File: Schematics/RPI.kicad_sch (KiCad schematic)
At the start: 9 parts, among them J1 RPi GPIO, U2 24LC256

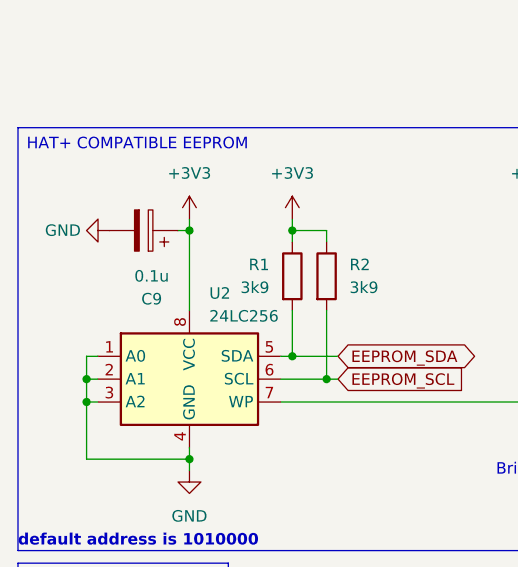
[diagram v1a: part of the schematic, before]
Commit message: Changed footprints, added 3d model to GPIO
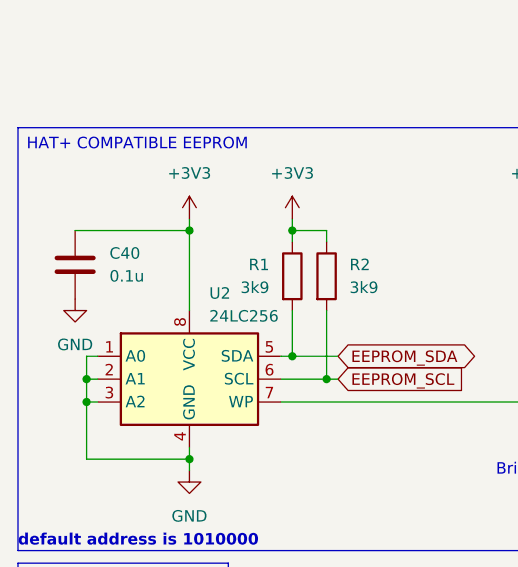
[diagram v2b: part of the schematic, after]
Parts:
- removed C9: 0.1u, Capacitor_SMD:C_0805_2012Metric_Pad1.18x1.45mm_HandSolder, symbol Device:C_Polarized
- added C40: 0.1u, Capacitor_SMD:C_0805_2012Metric_Pad1.18x1.45mm_HandSolder, symbol Device:C
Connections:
- net +3V3: now also C40.1
- net GND: now also C40.2
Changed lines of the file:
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@@
 	(wire
 		(pts
-			(xy 146.05 34.29) (xy 151.13 34.29)
+			(xy 22.86 55.88) (xy 35.56 55.88)
 		)
 		(stroke
@@
 	(wire
 		(pts
-			(xy 163.83 29.21) (xy 166.37 29.21)
+			(xy 146.05 34.29) (xy 151.13 34.29)
 		)
 		(stroke
@@
 	(wire
 		(pts
-			(xy 151.13 39.37) (xy 148.59 39.37)
+			(xy 163.83 29.21) (xy 166.37 29.21)
 		)
 		(stroke
@@
 	(wire
 		(pts
-			(xy 163.83 64.77) (xy 166.37 64.77)
+			(xy 151.13 39.37) (xy 148.59 39.37)
 		)
 		(stroke
@@
 	(wire
 		(pts
-			(xy 24.13 69.85) (xy 24.13 72.39)
+			(xy 163.83 64.77) (xy 166.37 64.77)
 		)
 		(stroke
@@
 	(wire
 		(pts
-			(xy 34.29 55.88) (xy 35.56 55.88)
+			(xy 24.13 69.85) (xy 24.13 72.39)
 		)
 		(stroke
@@
 	)
 	(symbol
-		(lib_id "Device:C_Polarized")
-		(at 30.48 55.88 270)
-		(mirror x)
-		(unit 1)
-		(exclude_from_sim no)
-		(in_bom yes)
-		(on_board yes)
-		(dnp no)
-		(property "Reference" "C9"
-			(at 31.369 63.5 90)
-			(effects
-				(font
-					(size 1.27 1.27)
-				)
-			)
-		)
-		(property "Value" "0.1u"
-			(at 31.369 60.96 90)
-			(effects
-				(font
-					(size 1.27 1.27)
-				)
-			)
-		)
-		(property "Footprint" "Capacitor_SMD:C_0805_2012Metric_Pad1.18x1.45mm_HandSolder"
-			(at 26.67 54.9148 0)
-			(effects
-				(font
-					(size 1.27 1.27)
-				)
-				(hide yes)
-			)
-		)
-		(property "Datasheet" "~"
-			(at 30.48 55.88 0)
-			(effects
-				(font
-					(size 1.27 1.27)
-				)
-				(hide yes)
-			)
-		)
-		(property "Description" "Polarized capacitor"
-			(at 30.48 55.88 0)
-			(effects
-				(font
-					(size 1.27 1.27)
-				)
-				(hide yes)
-			)
-		)
-		(pin "2"
-		)
-		(pin "1"
-		)
-		(instances
-			(project "Harmoniser HAT"
-				(path "/41751dd2-97f9-4cc6-b9e6-b561e5949053/94150540-adfd-4870-80d6-c5485bc02207"
-					(reference "C9")
-					(unit 1)
-				)
-			)
-		)
-	)
-	(symbol
 		(lib_id "power:+5V")
 		(at 166.37 27.94 0)
@@
 	)
 	(symbol
-		(lib_id "power:GND")
-		(at 26.67 55.88 270)
+		(lib_id "Device:R")
+		(at 22.86 118.11 180)
 		(unit 1)
 		(exclude_from_sim no)
@@
 		(on_board yes)
 		(dnp no)
-		(fields_autoplaced yes)
-		(property "Reference" "#PWR013"
-			(at 20.32 55.88 0)
+		(property "Reference" "R5"
+			(at 25.908 117.856 0)
 			(effects
 				(font
 					(size 1.27 1.27)
 				)
-				(hide yes)
 			)
 		)
-		(property "Value" "GND"
-			(at 23.495 55.8799 90)
+		(property "Value" "10k"
+			(at 22.86 118.11 90)
 			(effects
 				(font
 					(size 1.27 1.27)
 				)
-				(justify right)
 			)
 		)
-		(property "Footprint" ""
-			(at 26.67 55.88 0)
+		(property "Footprint" "Resistor_SMD:R_0805_2012Metric_Pad1.20x1.40mm_HandSolder"
+			(at 24.638 118.11 90)
 			(effects
 				(font
@@
 			)
 		)
-		(property "Datasheet" ""
-			(at 26.67 55.88 0)
+		(property "Datasheet" "~"
+			(at 22.86 118.11 0)
 			(effects
 				(font
@@
 			)
 		)
-		(property "Description" "Power symbol creates a global label with name \"GND\" , ground"
-			(at 26.67 55.88 0)
+		(property "Description" "Resistor"
+			(at 22.86 118.11 0)
 			(effects
 				(font
@@
 		(pin "1"
 		)
+		(pin "2"
+		)
 		(instances
 			(project "Harmoniser HAT"
 				(path "/41751dd2-97f9-4cc6-b9e6-b561e5949053/94150540-adfd-4870-80d6-c5485bc02207"
-					(reference "#PWR013")
+					(reference "R5")
 					(unit 1)
 				)
@@
 	(symbol
 		(lib_id "Device:R")
-		(at 22.86 118.11 180)
+		(at 22.86 106.68 180)
 		(unit 1)
 		(exclude_from_sim no)
@@
 		(on_board yes)
 		(dnp no)
-		(property "Reference" "R5"
-			(at 25.908 117.856 0)
+		(property "Reference" "R4"
+			(at 26.416 106.553 0)
 			(effects
 				(font
@@
 			)
 		)
-		(property "Value" "10k"
-			(at 22.86 118.11 90)
+		(property "Value" "22k"
+			(at 22.86 106.68 90)
 			(effects
 				(font
@@
 		)
 		(property "Footprint" "Resistor_SMD:R_0805_2012Metric_Pad1.20x1.40mm_HandSolder"
-			(at 24.638 118.11 90)
+			(at 24.638 106.68 90)
 			(effects
 				(font
@@
 		)
 		(property "Datasheet" "~"
-			(at 22.86 118.11 0)
+			(at 22.86 106.68 0)
 			(effects
 				(font
@@
 		)
 		(property "Description" "Resistor"
-			(at 22.86 118.11 0)
+			(at 22.86 106.68 0)
 			(effects
 				(font
@@
 			(project "Harmoniser HAT"
 				(path "/41751dd2-97f9-4cc6-b9e6-b561e5949053/94150540-adfd-4870-80d6-c5485bc02207"
-					(reference "R5")
+					(reference "R4")
 					(unit 1)
 				)
@@
 	)
 	(symbol
-		(lib_id "Device:R")
-		(at 22.86 106.68 180)
+		(lib_id "Device:C")
+		(at 22.86 59.69 0)
 		(unit 1)
 		(exclude_from_sim no)
@@
 		(on_board yes)
 		(dnp no)
-		(property "Reference" "R4"
-			(at 26.416 106.553 0)
+		(fields_autoplaced yes)
+		(property "Reference" "C40"
+			(at 26.67 58.4199 0)
 			(effects
 				(font
 					(size 1.27 1.27)
 				)
+				(justify left)
 			)
 		)
-		(property "Value" "22k"
-			(at 22.86 106.68 90)
+		(property "Value" "0.1u"
+			(at 26.67 60.9599 0)
 			(effects
 				(font
 					(size 1.27 1.27)
 				)
+				(justify left)
 			)
 		)
-		(property "Footprint" "Resistor_SMD:R_0805_2012Metric_Pad1.20x1.40mm_HandSolder"
-			(at 24.638 106.68 90)
+		(property "Footprint" "Capacitor_SMD:C_0805_2012Metric_Pad1.18x1.45mm_HandSolder"
+			(at 23.8252 63.5 0)
 			(effects
 				(font
@@
 		)
 		(property "Datasheet" "~"
-			(at 22.86 106.68 0)
+			(at 22.86 59.69 0)
 			(effects
 				(font
@@
 			)
 		)
-		(property "Description" "Resistor"
-			(at 22.86 106.68 0)
+		(property "Description" "Unpolarized capacitor"
+			(at 22.86 59.69 0)
 			(effects
 				(font
@@
 			(project "Harmoniser HAT"
 				(path "/41751dd2-97f9-4cc6-b9e6-b561e5949053/94150540-adfd-4870-80d6-c5485bc02207"
-					(reference "R4")
+					(reference "C40")
 					(unit 1)
 				)
@@
 					(unit 1)
 				)
+			)
+		)
+	)
+	(symbol
+		(lib_id "power:GND")
+		(at 22.86 63.5 0)
+		(unit 1)
+		(exclude_from_sim no)
+		(in_bom yes)
+		(on_board yes)
+		(dnp no)
+		(fields_autoplaced yes)
+		(property "Reference" "#PWR070"
+			(at 22.86 69.85 0)
+			(effects
+				(font
+					(size 1.27 1.27)
+				)
+				(hide yes)
+			)
+		)
+		(property "Value" "GND"
+			(at 22.86 68.58 0)
+			(effects
+				(font
+					(size 1.27 1.27)
+				)
+			)
+		)
+		(property "Footprint" ""
+			(at 22.86 63.5 0)
+			(effects
+				(font
+					(size 1.27 1.27)
+				)
+				(hide yes)
+			)
+		)
+		(property "Datasheet" ""
+			(at 22.86 63.5 0)
+			(effects
+				(font
+					(size 1.27 1.27)
+				)
+				(hide yes)
+			)
+		)
+		(property "Description" "Power symbol creates a global label with name \"GND\" , ground"
+			(at 22.86 63.5 0)
+			(effects
+				(font
+					(size 1.27 1.27)
+				)
+				(hide yes)
+			)
+		)
+		(pin "1"
+		)
+		(instances
+			(project "Harmoniser HAT"
+				(path "/41751dd2-97f9-4cc6-b9e6-b561e5949053/94150540-adfd-4870-80d6-c5485bc02207"
+					(reference "#PWR070")
+					(unit 1)
+				)

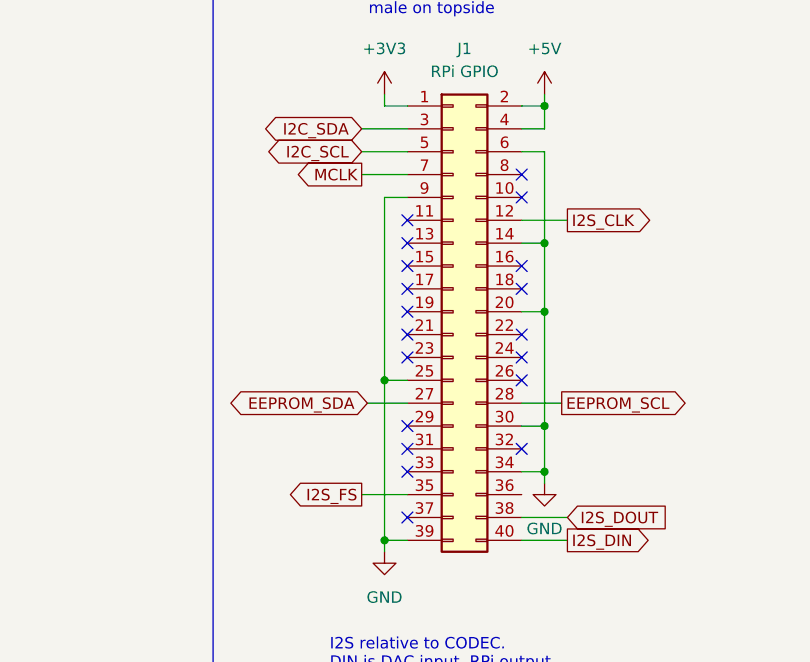
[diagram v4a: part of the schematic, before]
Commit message: Fix for Uni PCB
CODEC module, DIP package, and through-hole less components
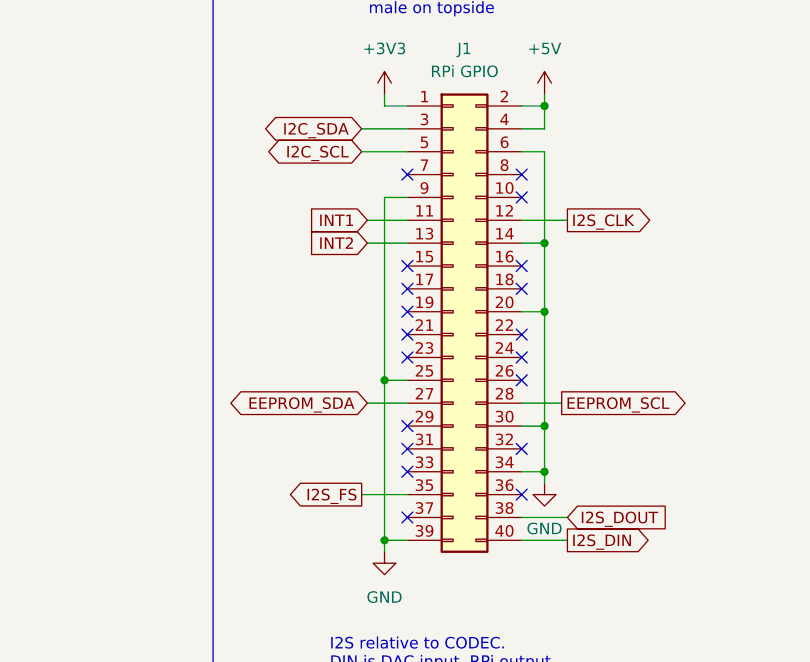
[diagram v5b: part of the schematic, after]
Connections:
- net INT1: now reaches J1.11 (Pin_11)
- net INT2: now reaches J1.13 (Pin_13)
- net MCLK: no longer names the net of J1.7 (Pin_7)
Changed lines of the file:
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@@
 	)
 	(no_connect
+		(at 151.13 36.83)
+	)
+	(no_connect
+		(at 163.83 72.39)
+	)
+	(no_connect
 		(at 163.83 36.83)
 	)
@@
 	)
 	(no_connect
-		(at 151.13 44.45)
-	)
-	(no_connect
 		(at 151.13 49.53)
 	)
@@
 	)
 	(no_connect
-		(at 151.13 41.91)
-	)
-	(no_connect
 		(at 163.83 59.69)
 	)
@@
 	(wire
 		(pts
+			(xy 146.685 41.91) (xy 151.13 41.91)
+		)
+		(stroke
+			(width 0)
+			(type default)
+		)
+	)
+	(wire
+		(pts
 			(xy 22.86 113.03) (xy 27.94 113.03)
 		)
@@
 	(wire
 		(pts
-			(xy 146.05 36.83) (xy 151.13 36.83)
-		)
-		(stroke
-			(width 0)
-			(type default)
-		)
-	)
-	(wire
-		(pts
 			(xy 22.86 110.49) (xy 22.86 113.03)
 		)
@@
 	(wire
 		(pts
+			(xy 146.685 44.45) (xy 151.13 44.45)
+		)
+		(stroke
+			(width 0)
+			(type default)
+		)
+	)
+	(wire
+		(pts
 			(xy 146.685 62.23) (xy 151.13 62.23)
 		)
@@
 			"AAAAAAAAAAAAAAAAAAAAAAAAAAAAAAAAAAAAAAAAAAAAAAAAAAAAAAAAAAAAAAAAAAAAAAAAAAAA"
 			"AAAAAAAAAAAAAAAAAAAAAAAAAAAAAAAAAAAAAAAAAAAAAAAAAAAAAAAAAAAAAAAAAAAAAAAAAAAA"
+			"AAAAAAAAAAAAAAAAAAAAAAAAAAAAAAAAAAAAAAAAAAAAAAAAAAAAAAAAAAAAAAAAAAAAAAAAAAAA"
+			"AAAAAAAAAAAAAAAAAAAAAAAAAAAAAAAAAAAAAAAAAAAAAAAAAAAAAAAAAAAAAAAAAAAAAAAAAAAA"
+			"AAAAAAAAAAAAAAAAAAAAAAAAAAAAAAAAAAAAAAAAAAAAAAAAAAAAAAAAAAAAAAAAAAAAAAAAAAAA"
+			"AAAAAAAAAAAAAAAAAAAAAAAAAAAAAAAAAAAAAAAAAAAAAAAAAAAAAAAAAAAAAAAAAAAAAAAAAAAA"
+			"AAAAAAAAAAAAAAAAAAAAAAAAAAAAAAAAAAAAAAAAAAAAAAAAAAAAAAAAAAAAAAAAAAAAAAAAAAAA"
+			"AAAAAAAAAAAAAAAAAAAAAAAAAAAAAAAAAAAAAAAAAAAAAAAAAAAAAAAAAAAAAAAAAAAAAAAAAAAA"
+			"AAAAAAAAAAAAAAAAAAAAAAAAAAAAAAAAAAAAAAAAAAAAAAAAAAAAAAAAAAAAAAAAAAAAAAAAAAAA"
+			"AAAAAAAAAAAAAAAAAAAAAAAAAAAAAAAAAAAAAAAAAAAAAAAAAAAAAAAAAAAAAAAAAAAAAAAAAAAA"
+			"AAAAAAAAAAAAAAAAAAAAAAAAAAAAAAAAAAAAAAAAAAAAAAAAAAAAAAAAAAAAAAAAAAAAAAAAAAAA"
+			"AAAAAAAAAAAAAAAAAAAAAAAAAAAAAAAAAAAAAAAAAAAAAAAAAAAAAAAAAAAAAAAAAAAAAAAAAAAA"
+			"AAAAAAAAAAAAAAAAAAAAAAAAAAAAAAAAAAAAAAAAAAAAAAAAAAAAAAAAAAAAAAAAAAAAAAAAAAAA"
+			"AAAAAAAAAAAAAAAAAAAAAAAAAAAAAAAAAAAAAAAAAAAAAAAAAAAAAAAAAAAAAAAAAAAAAAAAAAAA"
+			"AAAAAAAAAAAAAAAAAAAAAAAAAAAAAAAAAAAAAAAAAAAAAAAAAAAAAAAAAAAAAAAAAAAAAAAAAAAA"
+			"AAAAAAAAAAAAAAAAAAAAAAAAAAAAAAAAAAAAAAAAAAAAAAAAAAAAAAAAAAAAAAAAAAAAAAAAAAAA"
+			"AAAAAAAAAAAAAAAAAAAAAAAAAAAAAAAAAAAAAAAAAAAAAAAAAAAAAAAAAAAAAAAAAAAAAAAAAAAA"
+			"AAAAAAAAAAAAAAAAAAAAAAAAAAAAAAAAAAAAAAAAAAAAAAAAAAAAAAAAAAAAAAAAAAAAAAAAAAAA"
+			"AAAAAAAAAAAAAAAAAAAAAAAAAAAAAAAAAAAAAAAAAAAAAAAAAAAAAAAAAAAAAAAAAAAAAAAAAAAA"
+			"AAAAAAAAAAAAAAAAAAAAAAAAAAAAAAAAAAAAAAAAAAAAAAAAAAAAAAAAAAAAAAAAAAAAAAAAAAAA"
 			"AAAAAAAAAAAAAAAAAAAAAA=="
 		)
@@
 			"AAAAAAAAAAAAAAAAAAAAAAAAAAAAAAAAAAAAAAAAAAAAAAAAAAAAAAAAAAAAAAAAAAAAAAAAAAAA"
 			"AAAAAAAAAAAAAAAAAAAAAAAAAAAAAAAAAAAAAAAAAAAAAAAAAAAAAAAAAAAAAAAAAAAAAAAAAAAA"
+			"AAAAAAAAAAAAAAAAAAAAAAAAAAAAAAAAAAAAAAAAAAAAAAAAAAAAAAAAAAAAAAAAAAAAAAAAAAAA"
+			"AAAAAAAAAAAAAAAAAAAAAAAAAAAAAAAAAAAAAAAAAAAAAAAAAAAAAAAAAAAAAAAAAAAAAAAAAAAA"
+			"AAAAAAAAAAAAAAAAAAAAAAAAAAAAAAAAAAAAAAAAAAAAAAAAAAAAAAAAAAAAAAAAAAAAAAAAAAAA"
+			"AAAAAAAAAAAAAAAAAAAAAAAAAAAAAAAAAAAAAAAAAAAAAAAAAAAAAAAAAAAAAAAAAAAAAAAAAAAA"
+			"AAAAAAAAAAAAAAAAAAAAAAAAAAAAAAAAAAAAAAAAAAAAAAAAAAAAAAAAAAAAAAAAAAAAAAAAAAAA"
+			"AAAAAAAAAAAAAAAAAAAAAAAAAAAAAAAAAAAAAAAAAAAAAAAAAAAAAAAAAAAAAAAAAAAAAAAAAAAA"
+			"AAAAAAAAAAAAAAAAAAAAAAAAAAAAAAAAAAAAAAAAAAAAAAAAAAAAAAAAAAAAAAAAAAAAAAAAAAAA"
+			"AAAAAAAAAAAAAAAAAAAAAAAAAAAAAAAAAAAAAAAAAAAAAAAAAAAAAAAAAAAAAAAAAAAAAAAAAAAA"
+			"AAAAAAAAAAAAAAAAAAAAAAAAAAAAAAAAAAAAAAAAAAAAAAAAAAAAAAAAAAAAAAAAAAAAAAAAAAAA"
+			"AAAAAAAAAAAAAAAAAAAAAAAAAAAAAAAAAAAAAAAAAAAAAAAAAAAAAAAAAAAAAAAAAAAAAAAAAAAA"
+			"AAAAAAAAAAAAAAAAAAAAAAAAAAAAAAAAAAAAAAAAAAAAAAAAAAAAAAAAAAAAAAAAAAAAAAAAAAAA"
+			"AAAAAAAAAAAAAAAAAAAAAAAAAAAAAAAAAAAAAAAAAAAAAAAAAAAAAAAAAAAAAAAAAAAAAAAAAAAA"
+			"AAAAAAAAAAAAAAAAAAAAAAAAAAAAAAAAAAAAAAAAAAAAAAAAAAAAAAAAAAAAAAAAAAAAAAAAAAAA"
+			"AAAAAAAAAAAAAAAAAAAAAAAAAAAAAAAAAAAAAAAAAAAAAAAAAAAAAAAAAAAAAAAAAAAAAAAAAAAA"
+			"AAAAAAAAAAAAAAAAAAAAAAAAAAAAAAAAAAAAAAAAAAAAAAAAAAAAAAAAAAAAAAAAAAAAAAAAAAAA"
+			"AAAAAAAAAAAAAAAAAAAAAAAAAAAAAAAAAAAAAAAAAAAAAAAAAAAAAAAAAAAAAAAAAAAAAAAAAAAA"
+			"AAAAAAAAAAAAAAAAAAAAAAAAAAAAAAAAAAAAAAAAAAAAAAAAAAAAAAAAAAAAAAAAAAAAAAAAAAAA"
+			"AAAAAAAAAAAAAAAAAAAAAAAAAAAAAAAAAAAAAAAAAAAAAAAAAAAAAAAAAAAAAAAAAAAAAAAAAAAA"
 			"AAAAAAAAAAAAAAAAAAAAAAAAAAAAAAAAAA=="
 		)
 	)
+	(global_label "INT2"
+		(shape input)
+		(at 146.685 44.45 180)
+		(fields_autoplaced yes)
+		(effects
+			(font
+				(size 1.27 1.27)
+			)
+			(justify right)
+		)
+		(property "Intersheetrefs" "${INTERSHEET_REFS}"
+			(at 139.5874 44.45 0)
+			(effects
+				(font
+					(size 1.27 1.27)
+				)
+				(justify right)
+				(hide yes)
+			)
+		)
+	)
 	(global_label "EEPROM_SDA"
 		(shape bidirectional)
@@
 		)
 	)
-	(global_label "MCLK"
-		(shape output)
-		(at 146.05 36.83 180)
+	(global_label "INT1"
+		(shape input)
+		(at 146.685 41.91 180)
 		(fields_autoplaced yes)
 		(effects
@@
 		)
 		(property "Intersheetrefs" "${INTERSHEET_REFS}"
-			(at 138.0453 36.83 0)
+			(at 139.5874 41.91 0)
 			(effects
 				(font

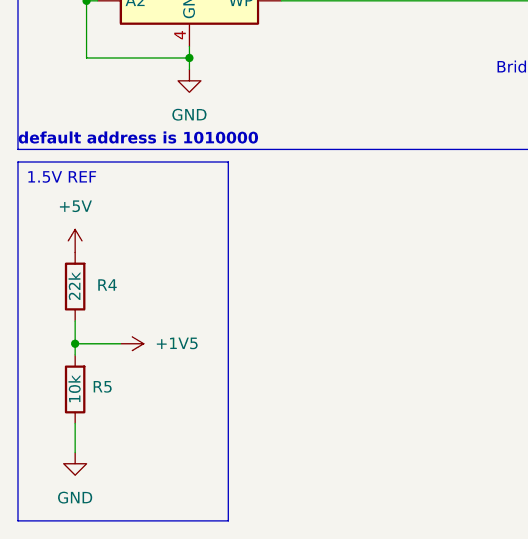
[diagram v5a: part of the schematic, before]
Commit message: Finished PCB routing
New Layout fits perfectly, now all the parts are through-hole and routed together. 20 Vias is a nightmare but better than what we started with
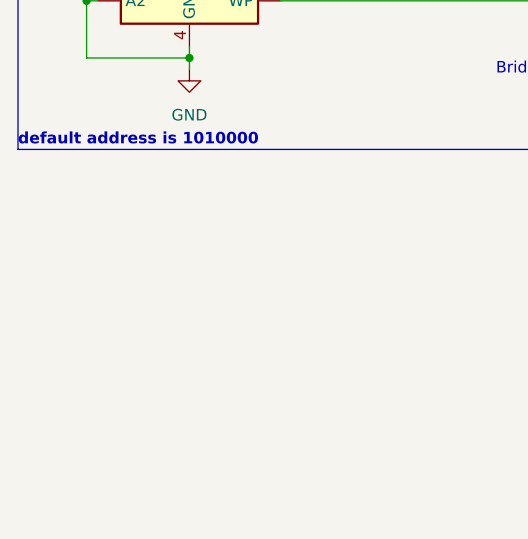
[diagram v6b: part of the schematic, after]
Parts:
- removed R4: 22k, Resistor_SMD:R_0805_2012Metric_Pad1.20x1.40mm_HandSolder, symbol Device:R
- removed R5: 10k, Resistor_SMD:R_0805_2012Metric_Pad1.20x1.40mm_HandSolder, symbol Device:R
- C40: footprint Capacitor_SMD:C_0805_2012Metric_Pad1.18x1.45mm_HandSolder -> Capacitor_THT:C_Disc_D4.7mm_W2.5mm_P5.00mm
- R1, R2, R3: footprint Resistor_SMD:R_0805_2012Metric_Pad1.20x1.40mm_HandSolder -> Resistor_THT:R_Axial_DIN0207_L6.3mm_D2.5mm_P10.16mm_Horizontal

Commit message: Tidied up Schematic
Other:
- note added: "I2S named relative to CODEC. DIN is DAC input, RPi output. DOUT is ADC output, RPi input."
- note removed: "I2S relative to CODEC. DIN is DAC input, RPi output. DOUT is ADC output, RPi input."
- moved on the sheet: C40, JP1, R1, R2, R3, U2
